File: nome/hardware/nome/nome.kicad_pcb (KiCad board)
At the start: 2 copper layers, 59 parts, among them J1 SJ-2524, J2 JTAG_SWD, J3 JST, J4 7SEG_DEBUG, SW1 SW_SPDT, SW2 Rotary_Encoder_Switch, U1 LM1117-1.8, U2 LM1117-3.3, U3 AS1115, U4 STMF411CEU6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

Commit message: More PCB layout
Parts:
- moved D4 139.8 mm to (48.8, 154.4)
- moved R5 139.2 mm to (58.4, 154.4)
- moved R2 113.3 mm to (57.9, 138.2)
- moved U7 108.9 mm to (40.1, 126.5), turned to 90 degrees
- moved R4 106.7 mm to (58.4, 148.8)
- moved D2 105.9 mm to (49.3, 143.8)
- moved D3 105.1 mm to (49.3, 148.8)
- moved C17 104.9 mm to (105.7, 147.3), turned to 180 degrees
- moved C16 104.8 mm to (105.7, 150.9), turned to 180 degrees
- moved R6 100.5 mm to (93.5, 152.9), turned to 180 degrees
- moved SW1 97.7 mm to (178.8, 121.4)
- moved R3 95.8 mm to (57.9, 143.3)
- moved C21 91.4 mm to (113.3, 132.1), turned to 180 degrees
- moved C9 91.0 mm to (93.5, 148.8)
- moved C12 90.0 mm to (96.5, 131.6), turned to 90 degrees
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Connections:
- C13 pad 2: Net-(C13-Pad2) -> GND
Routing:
- net GND: track 0.00 -> 80.5 mm
- net +1V8: track 0.00 -> 54.8 mm
- net +3V3: track 3.90 -> 41.3 mm, vias 0 -> 2
- net /HP_B: track 0.00 -> 30.1 mm, vias 0 -> 2
- net /HP_A: track 0.00 -> 23.7 mm, vias 0 -> 2
- net Net-(C28-Pad1): track 0.00 -> 20.6 mm
- net /SPKR_HP: track 0.00 -> 19.3 mm, vias 0 -> 2
- net Net-(C24-Pad1): track 0.00 -> 12.1 mm
- net Net-(C22-Pad1): track 0.00 -> 8.32 mm
- net Net-(C18-Pad2): track 0.00 -> 7.87 mm
- net Net-(C20-Pad2): track 0.00 -> 7.25 mm
- net Net-(C15-Pad2): track 0.00 -> 6.48 mm
- net Net-(C13-Pad1): track 0.00 -> 6.41 mm
- net Net-(C10-Pad1): track 0.00 -> 5.12 mm
- net Net-(C26-Pad2): track 0.00 -> 4.75 mm
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
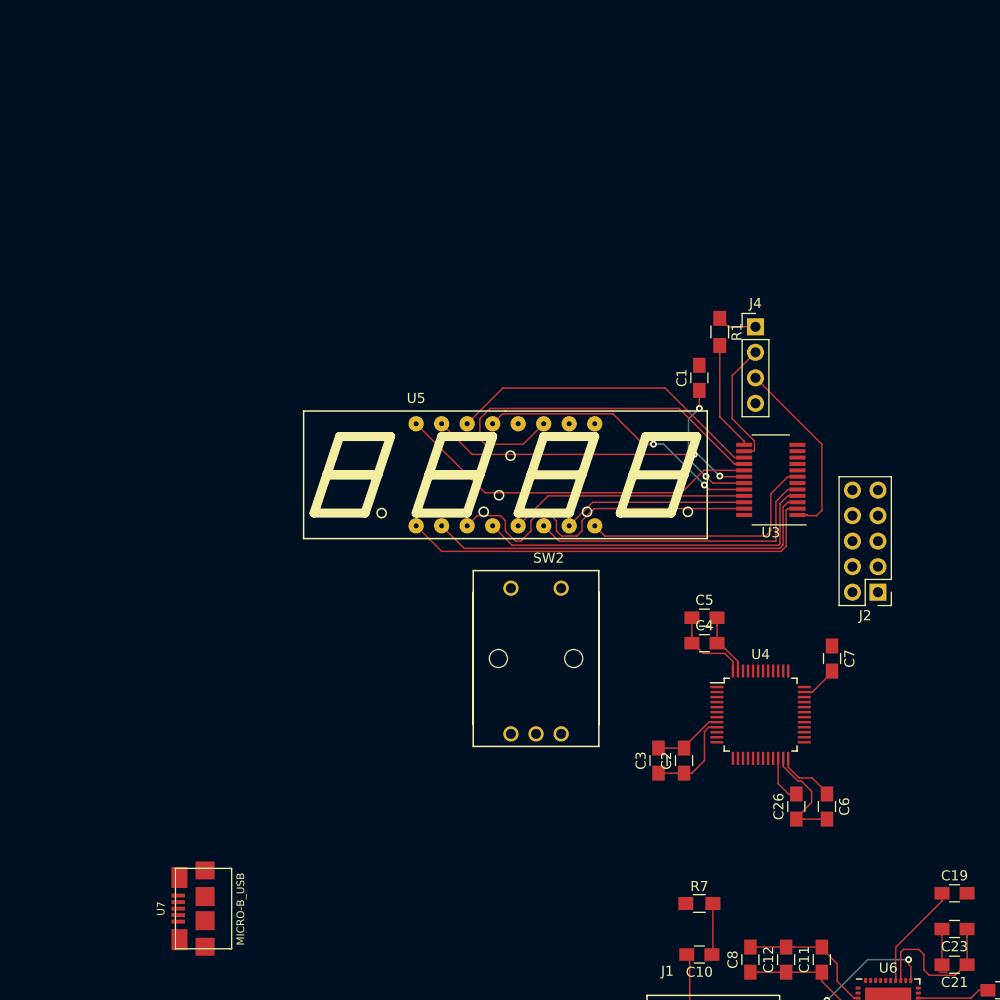
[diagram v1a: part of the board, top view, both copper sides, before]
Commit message: Add PCB outline
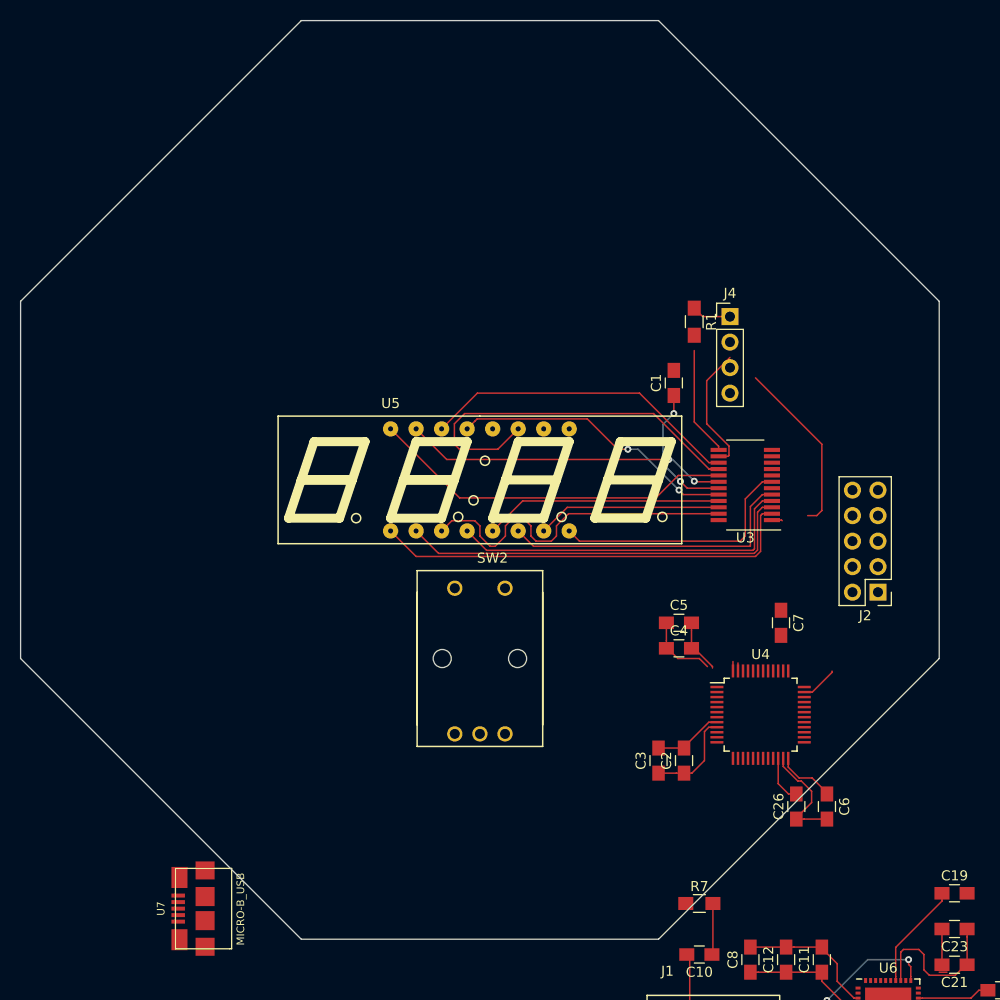
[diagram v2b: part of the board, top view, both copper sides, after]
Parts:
- moved C7 6.20 mm to (96.0, 98.0)
- moved SW2 5.59 mm to (66.0, 101.6)
- moved J4 2.74 mm to (90.9, 67.6)
- moved R1 2.74 mm to (87.4, 68.1)
- moved C1 2.59 mm to (85.3, 74.2)
- moved C4 2.59 mm to (85.9, 100.6)
- moved U3 2.59 mm to (92.5, 84.3)
- moved C5 2.59 mm to (85.9, 98.0)
- moved U5 2.59 mm to (66.0, 83.8)
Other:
- board outline added: 91.4 x 91.4 mm

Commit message: Layout all non ground plane nets
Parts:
- moved R9 116.9 mm to (42.2, 96.5), turned to 0 degrees
- moved U8 116.4 mm to (48.3, 102.1)
- moved C29 116.3 mm to (48.3, 107.2)
- moved C28 116.3 mm to (48.3, 110.7)
- moved R10 115.3 mm to (54.9, 101.1)
- moved J3 113.8 mm to (50.8, 120.9)
- moved D6 110.9 mm to (48.3, 96.5)
- moved D5 110.3 mm to (48.3, 93.0)
- moved R8 108.8 mm to (42.2, 93.0)
- moved LS1 106.0 mm to (58.4, 53.3), turned to 180 degrees
- moved C27 102.8 mm to (54.9, 107.2), turned to 0 degrees
- moved U2 92.0 mm to (71.1, 120.4)
- moved C21 90.9 mm to (78.2, 48.3)
- moved C16 90.9 mm to (70.6, 67.1)
- moved C20 90.9 mm to (82.8, 50.8)
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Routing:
- net +1V8: track 54.8 -> 293.3 mm, vias 0 -> 6
- net +3V3: track 41.3 -> 268.8 mm, vias 2 -> 13
- net Net-(J3-Pad2): track 0.00 -> 107.7 mm, vias 0 -> 2
- net /LED_Err: track 0.00 -> 94.0 mm
- net /LED_Act: track 0.00 -> 89.4 mm
- net GND: track 80.5 -> 167.3 mm, vias 0 -> 9
- net /LED_Ok: track 0.00 -> 84.6 mm, vias 0 -> 2
- net /7SEG_SCL: track 12.7 -> 94.6 mm, vias 0 -> 4
- net /DAC_CK: track 0.00 -> 81.3 mm, vias 0 -> 2
- net /DAC_MCK: track 0.00 -> 79.9 mm, vias 0 -> 2
- net /DAC_WS: track 0.00 -> 76.4 mm, vias 0 -> 2
- net /DAC_RST: track 0.00 -> 74.9 mm, vias 0 -> 2
- net /7SEG_SDA: track 18.6 -> 92.7 mm, vias 0 -> 4
- net /DAC_SD: track 0.00 -> 71.5 mm, vias 0 -> 2
- net Net-(C27-Pad1): track 0.00 -> 50.2 mm, vias 0 -> 2
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
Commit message: Add ground plane to back
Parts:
- turned C21 to 0 degrees
- turned C23 to 0 degrees
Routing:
- net GND: track 167.3 -> 264.4 mm, vias 9 -> 23
- net +1V8: track 293.3 -> 317.2 mm
- net +3V3: track 268.8 -> 292.5 mm, vias 13 -> 15
- added copper zone on B.Cu, net GND

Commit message: Connect remaining nets
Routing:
- net +1V8: track 317.2 -> 309.7 mm
- net GND: track 264.4 -> 268.0 mm
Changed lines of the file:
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@@
   (thickness 1.6)
   (drawings 8)
-  (tracks 923)
+  (tracks 922)
   (zones 0)
   (modules 59)
@@
       (effects (font (size 1 1) (thickness 0.15)))
     )
+    (fp_line (start 2.35 0.9) (end -2.35 0.9) (layer F.CrtYd) (width 0.05))
+    (fp_line (start 2.35 0.9) (end 2.35 -0.9) (layer F.CrtYd) (width 0.05))
+    (fp_line (start -2.35 -0.9) (end -2.35 0.9) (layer F.CrtYd) (width 0.05))
+    (fp_line (start -2.35 -0.9) (end 2.35 -0.9) (layer F.CrtYd) (width 0.05))
+    (fp_line (start -0.6 -0.88) (end 0.6 -0.88) (layer F.SilkS) (width 0.12))
+    (fp_line (start 0.6 0.88) (end -0.6 0.88) (layer F.SilkS) (width 0.12))
+    (fp_line (start -1 -0.62) (end 1 -0.62) (layer F.Fab) (width 0.1))
+    (fp_line (start 1 -0.62) (end 1 0.62) (layer F.Fab) (width 0.1))
+    (fp_line (start 1 0.62) (end -1 0.62) (layer F.Fab) (width 0.1))
+    (fp_line (start -1 0.62) (end -1 -0.62) (layer F.Fab) (width 0.1))
     (fp_text user %R (at 0 0) (layer F.Fab)
       (effects (font (size 0.5 0.5) (thickness 0.075)))
     )
-    (fp_line (start -1 0.62) (end -1 -0.62) (layer F.Fab) (width 0.1))
-    (fp_line (start 1 0.62) (end -1 0.62) (layer F.Fab) (width 0.1))
-    (fp_line (start 1 -0.62) (end 1 0.62) (layer F.Fab) (width 0.1))
-    (fp_line (start -1 -0.62) (end 1 -0.62) (layer F.Fab) (width 0.1))
-    (fp_line (start 0.6 0.88) (end -0.6 0.88) (layer F.SilkS) (width 0.12))
-    (fp_line (start -0.6 -0.88) (end 0.6 -0.88) (layer F.SilkS) (width 0.12))
-    (fp_line (start -2.35 -0.9) (end 2.35 -0.9) (layer F.CrtYd) (width 0.05))
-    (fp_line (start -2.35 -0.9) (end -2.35 0.9) (layer F.CrtYd) (width 0.05))
-    (fp_line (start 2.35 0.9) (end 2.35 -0.9) (layer F.CrtYd) (width 0.05))
-    (fp_line (start 2.35 0.9) (end -2.35 0.9) (layer F.CrtYd) (width 0.05))
-    (pad 1 smd rect (at -1.35 0) (size 1.5 1.3) (layers F.Cu F.Paste F.Mask)
-      (net 106 GND))
     (pad 2 smd rect (at 1.35 0) (size 1.5 1.3) (layers F.Cu F.Paste F.Mask)
       (net 6 "Net-(C10-Pad1)"))
+    (pad 1 smd rect (at -1.35 0) (size 1.5 1.3) (layers F.Cu F.Paste F.Mask)
+      (net 106 GND))
     (model ${KISYS3DMOD}/Resistors_SMD.3dshapes/R_0805.wrl
       (at (xyz 0 0 0))
@@
   (segment (start 79.756 108.1994) (end 79.756 105.3176) (width 0.1524) (layer F.Cu) (net 1))
   (segment (start 79.756 105.3176) (end 80.1916 104.882) (width 0.1524) (layer F.Cu) (net 1))
+  (segment (start 75.184 47.752) (end 75.692 48.26) (width 0.1524) (layer F.Cu) (net 2))
+  (segment (start 75.692 48.26) (end 76.982 48.26) (width 0.1524) (layer F.Cu) (net 2))
+  (segment (start 75.184 47.244) (end 75.184 47.752) (width 0.1524) (layer F.Cu) (net 2))
   (segment (start 68.628 54.082) (end 62.153482 54.082) (width 0.1524) (layer F.Cu) (net 2))
   (segment (start 62.153482 54.082) (end 61.371482 54.864) (width 0.1524) (layer F.Cu) (net 2))
@@
   (segment (start 74.676 46.736) (end 73.152 46.736) (width 0.1524) (layer F.Cu) (net 2))
   (segment (start 75.184 47.244) (end 74.676 46.736) (width 0.1524) (layer F.Cu) (net 2))
-  (segment (start 75.184 48.768) (end 75.184 47.244) (width 0.1524) (layer F.Cu) (net 2))
-  (segment (start 75.72281 49.30681) (end 75.184 48.768) (width 0.1524) (layer F.Cu) (net 2))
-  (segment (start 79.482 48.26) (end 79.357 48.26) (width 0.1524) (layer F.Cu) (net 2))
-  (segment (start 79.357 48.26) (end 78.31019 49.30681) (width 0.1524) (layer F.Cu) (net 2))
-  (segment (start 78.31019 49.30681) (end 75.72281 49.30681) (width 0.1524) (layer F.Cu) (net 2))
+  (segment (start 79.482 48.26) (end 79.357 48.26) (width 0.1524) (layer F.Cu) (net 106))
   (segment (start 71.862 63.5) (end 71.737 63.5) (width 0.1524) (layer F.Cu) (net 2))
   (segment (start 71.737 63.5) (end 70.378 62.141) (width 0.1524) (layer F.Cu) (net 2))
@@
   (segment (start 71.862 63.5) (end 71.862 55.848) (width 0.1524) (layer F.Cu) (net 2))
   (segment (start 71.862 55.848) (end 71.878 55.832) (width 0.1524) (layer F.Cu) (net 2))
-  (segment (start 79.482 44.704) (end 79.482 45.4814) (width 0.1524) (layer F.Cu) (net 2))
-  (segment (start 79.482 45.4814) (end 79.482 48.26) (width 0.1524) (layer F.Cu) (net 2))
   (segment (start 76.982 41.148) (end 76.982 41.9254) (width 0.1524) (layer F.Cu) (net 2))
   (segment (start 76.982 41.9254) (end 72.378 46.5294) (width 0.1524) (layer F.Cu) (net 2))
@@
   (segment (start 69.878 47.018) (end 69.596 46.736) (width 0.1524) (layer F.Cu) (net 85))
   (via (at 69.596 46.736) (size 0.6858) (drill 0.3302) (layers F.Cu B.Cu) (net 85))
+  (segment (start 79.482 44.704) (end 79.482 47.828934) (width 0.1524) (layer F.Cu) (net 106))
+  (segment (start 79.482 47.828934) (end 79.697533 48.044467) (width 0.1524) (layer F.Cu) (net 106))
   (segment (start 61.468 46.502) (end 65.024 46.502) (width 0.1524) (layer F.Cu) (net 106))
   (segment (start 57.912 46.502) (end 61.468 46.502) (width 0.1524) (layer F.Cu) (net 106))
